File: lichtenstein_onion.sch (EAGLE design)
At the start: 49 parts, among them IC1 LM2852Y-3V3, J1 MAGJACK, U1 ONION-OMEGA2

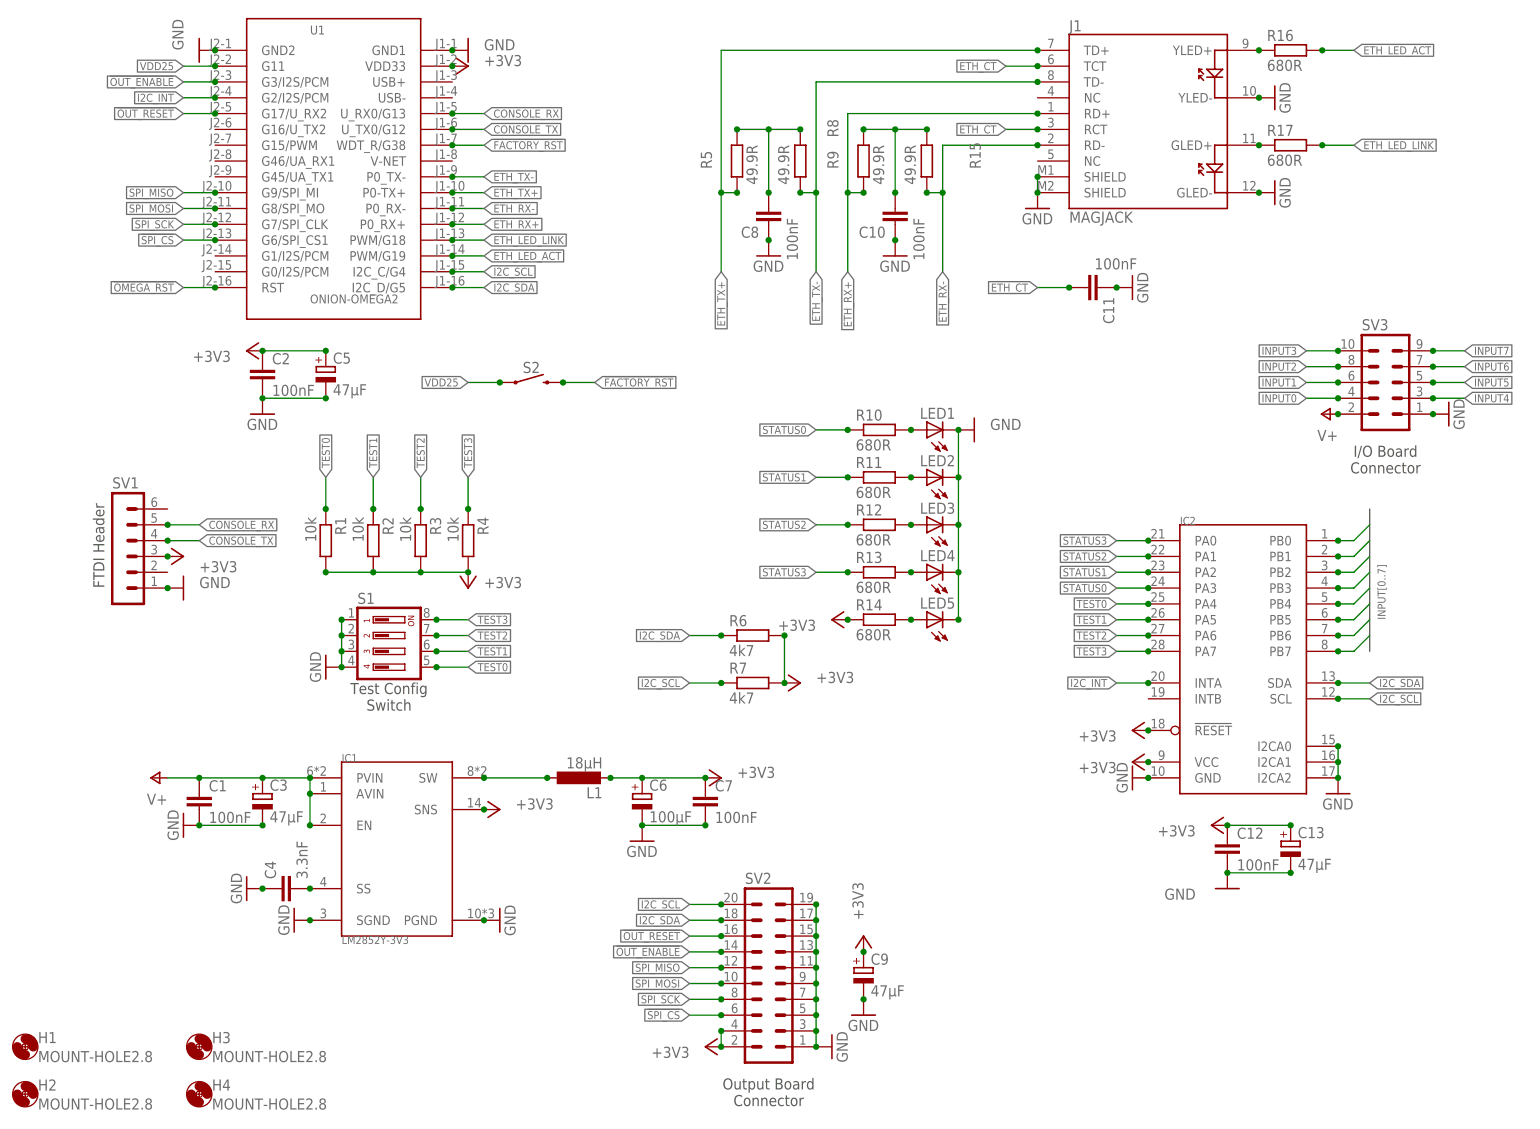
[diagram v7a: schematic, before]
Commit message: Cleaned up output board; added pull-ups to inputs on Lichtenstein board; moved some decoupling caps on FPGA output board
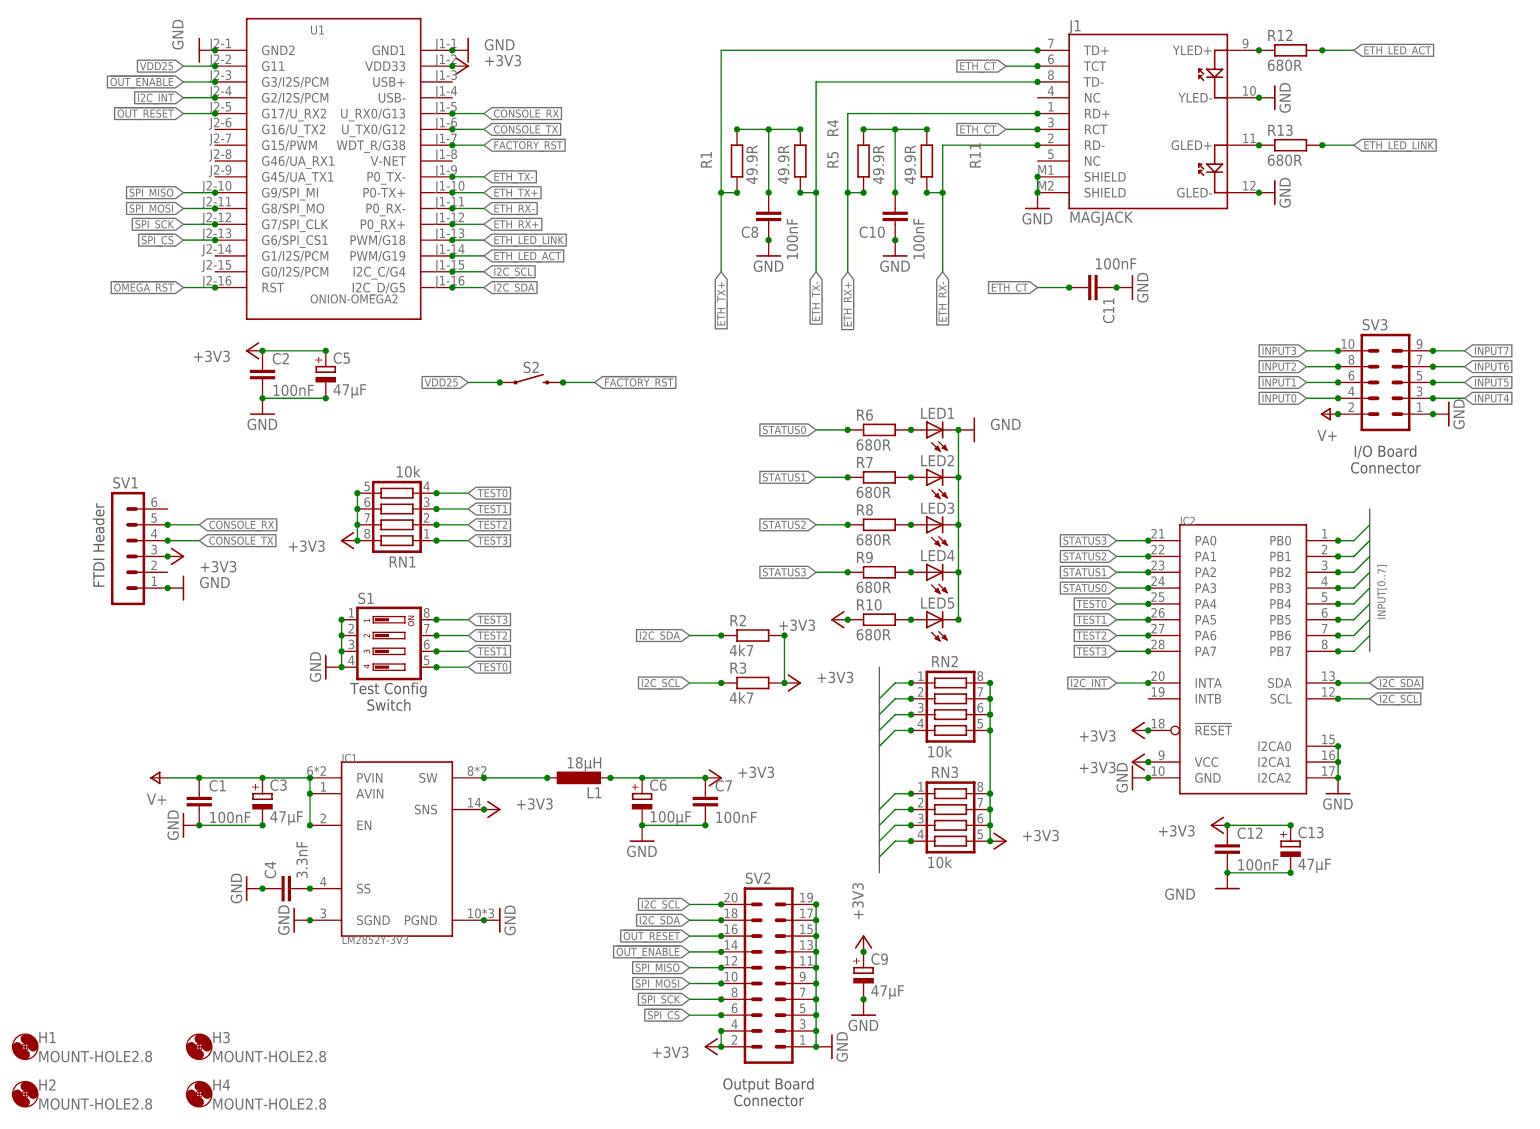
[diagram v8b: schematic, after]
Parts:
- removed R14, R16, R17: 680R, rcl:R-EU_M0805
- removed R15: 49.9R, rcl:R-EU_M0805
- added RN1, RN2, RN3: 10k, resistor-net:CTS742C083
- R1: value 10k -> 49.9R; MOUSER 652-CR0805FX-1002ELF -> 652-CR0805FX-49R9ELF
- R11: value 680R -> 49.9R; MOUSER 652-CR0805-FX6800GLF -> 652-CR0805FX-49R9ELF
- R2, R3: value 10k -> 4k7; MOUSER 652-CR0805FX-1002ELF -> 652-CR0805-FX4701GLF
- R4: value 10k -> 49.9R; MOUSER 652-CR0805FX-1002ELF -> 652-CR0805-FX4701GLF
- R6, R7: value 4k7 -> 680R; MOUSER 652-CR0805-FX4701GLF -> 652-CR0805-FX6800GLF
- R8: value 49.9R -> 680R; MOUSER 652-CR0805-FX4701GLF -> 652-CR0805-FX6800GLF
- R9: value 49.9R -> 680R; MOUSER 652-CR0805FX-49R9ELF -> 652-CR0805-FX6800GLF
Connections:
- net +3V3: now also R10.1, RN1.5, RN1.6, RN1.7, RN1.8, RN2.5, RN2.6, RN2.7, RN2.8, RN3.5, RN3.6, RN3.7, RN3.8; no longer R1.2, R14.1, R4.2, R6.2, R7.2
- net ETH_LED_ACT: now also R12.2; no longer R16.2
- net ETH_LED_LINK: now also R13.2; no longer R17.2
- net ETH_RX+: now also R5.1; no longer R9.1
- net ETH_RX-: now also R11.1; no longer R15.1
- net ETH_TX+: now also R1.1; no longer R5.1
- net ETH_TX-: now also R4.1; no longer R8.1
- net I2C_SCL: now also R3.1; no longer R7.1
- net I2C_SDA: now also R2.1; no longer R6.1
- net INPUT0: now also RN2.1
- net INPUT1: now also RN2.2
- net INPUT2: now also RN2.3
- net INPUT3: now also RN2.4
- net INPUT4: now also RN3.4
- net INPUT5: now also RN3.3
- net INPUT6: now also RN3.2
- net INPUT7: now also RN3.1
- net N$1: now also R10.2; no longer R14.2
- net N$10: now also R8.2; no longer R12.2
- net N$11: now also R9.2; no longer R13.2
- net N$2: now also R6.2; no longer R10.2
- net N$3: now also R1.2, R4.2; no longer R5.2, R8.2
- net N$4: now also R12.1; no longer R16.1
- net N$5: now also R13.1; no longer R17.1
- net N$6: now also R11.2, R5.2; no longer R15.2, R9.2
- net N$9: now also R7.2; no longer R11.2
- net STATUS0: now also R6.1; no longer R10.1
- net STATUS1: now also R7.1; no longer R11.1
- net STATUS2: now also R8.1; no longer R12.1
- net STATUS3: now also R9.1; no longer R13.1
- net TEST0: now also RN1.4; no longer R1.1
- net TEST1: now also RN1.3; no longer R2.1
- net TEST2: now also RN1.2; no longer R3.1
- net TEST3: now also RN1.1; no longer R4.1
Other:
- moved on the sheet: R1, R10, R11, R12, R13, R2, R3, R4, R5, R6, R7, R8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
